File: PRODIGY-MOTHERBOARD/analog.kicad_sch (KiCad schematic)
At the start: 5 parts, among them U16 LM386

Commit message: CAN schematic done
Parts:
- renumbered R15 to R64, RV1 to RV3, U16 to U24
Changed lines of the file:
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@@
 		(dnp no)
 		(fields_autoplaced yes)
-		(property "Reference" "U16"
+		(property "Reference" "U24"
 			(at 72.39 140.0811 0)
 			(effects
@@
 			(project "PRODIGY-MOTHERBOARD"
 				(path "/f1c25860-8989-4190-bd24-2491d23ca7d9/a2bc12b1-b9d0-4419-aed0-74588fb36767"
-					(reference "U16")
+					(reference "U24")
 					(unit 1)
 				)
@@
 		(dnp no)
 		(fields_autoplaced yes)
-		(property "Reference" "RV1"
+		(property "Reference" "RV3"
 			(at 115.57 95.885 0)
 			(effects
@@
 			(project "PRODIGY-MOTHERBOARD"
 				(path "/f1c25860-8989-4190-bd24-2491d23ca7d9/a2bc12b1-b9d0-4419-aed0-74588fb36767"
-					(reference "RV1")
+					(reference "RV3")
 					(unit 1)
 				)
@@
 		(dnp no)
 		(fields_autoplaced yes)
-		(property "Reference" "R15"
+		(property "Reference" "R64"
 			(at 196.85 95.885 0)
 			(effects
@@
 			(project "PRODIGY-MOTHERBOARD"
 				(path "/f1c25860-8989-4190-bd24-2491d23ca7d9/a2bc12b1-b9d0-4419-aed0-74588fb36767"
-					(reference "R15")
-					(unit 1)
-				)
+					(reference "R64")
+					(unit 1)
+				)

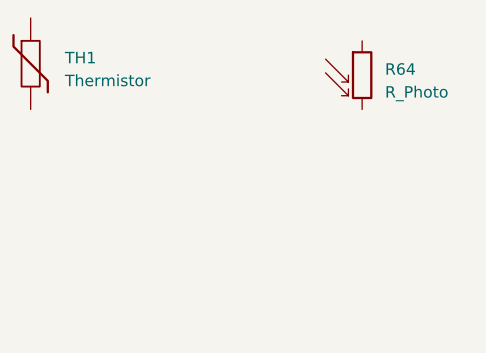
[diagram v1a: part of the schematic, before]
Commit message: SPI NFC schematic done.
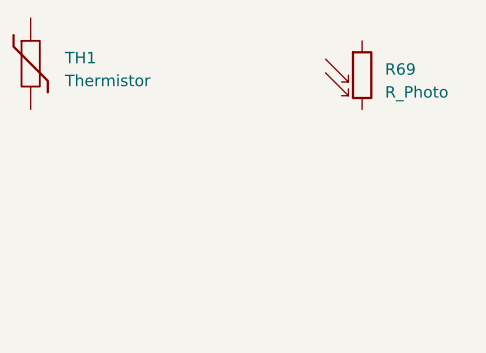
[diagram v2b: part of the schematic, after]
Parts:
- renumbered R64 to R69
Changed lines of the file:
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@@
 		(dnp no)
 		(fields_autoplaced yes)
-		(property "Reference" "R64"
+		(property "Reference" "R69"
 			(at 196.85 95.885 0)
 			(effects
@@
 			(project "PRODIGY-MOTHERBOARD"
 				(path "/f1c25860-8989-4190-bd24-2491d23ca7d9/a2bc12b1-b9d0-4419-aed0-74588fb36767"
-					(reference "R64")
+					(reference "R69")
 					(unit 1)
 				)

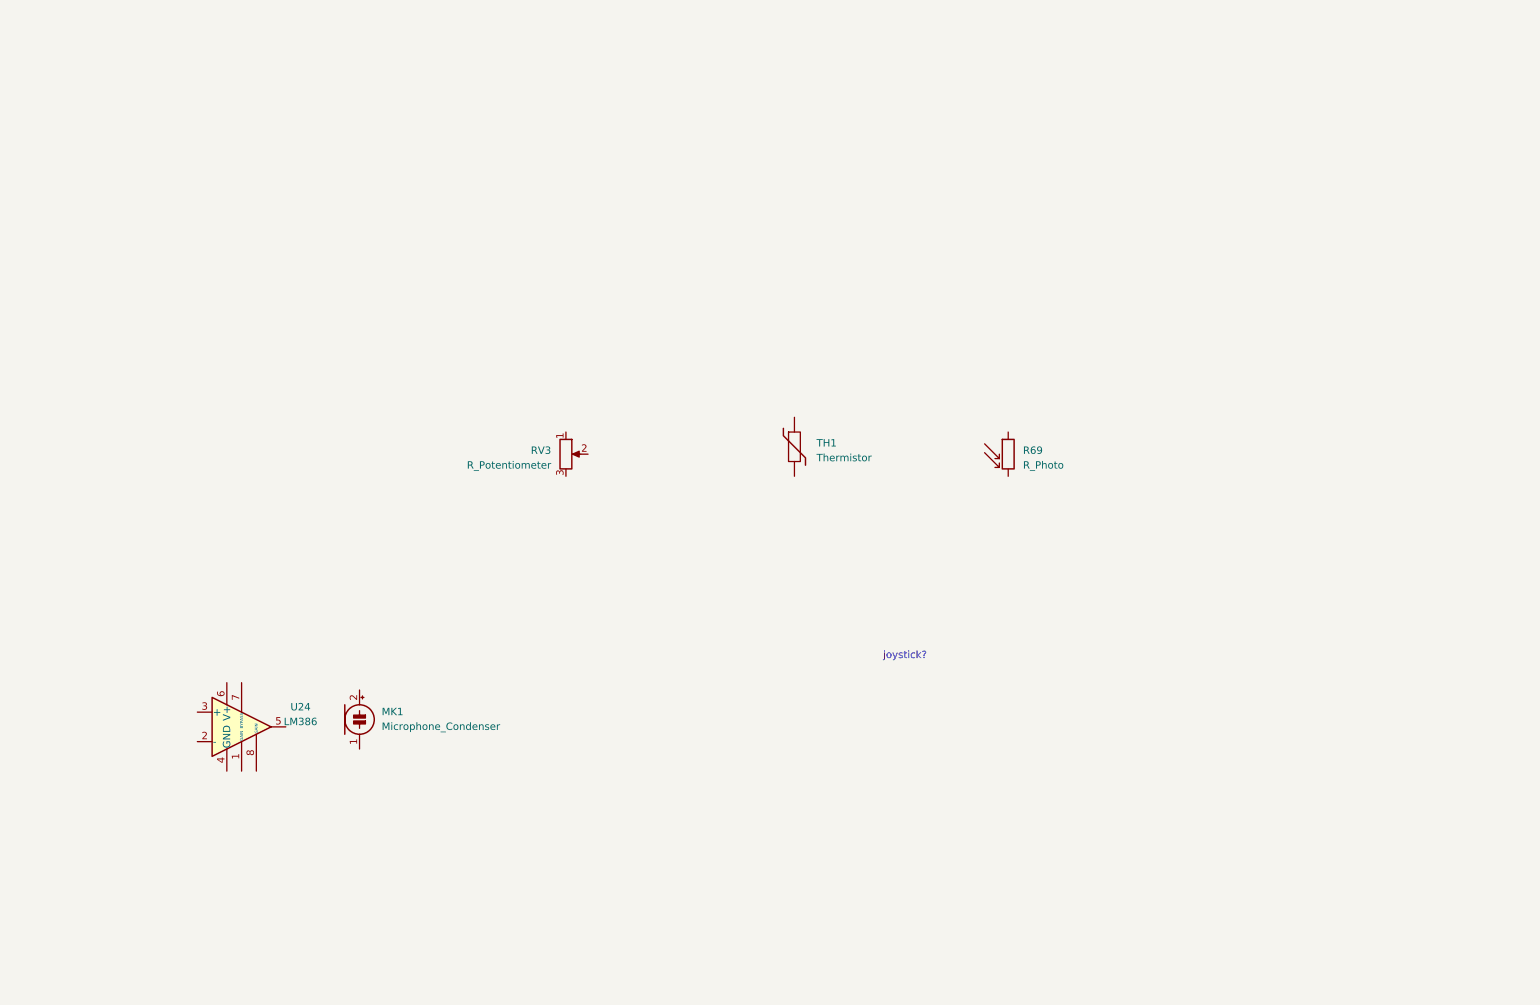
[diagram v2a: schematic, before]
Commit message: Analog schematic finished, except the joystick part.
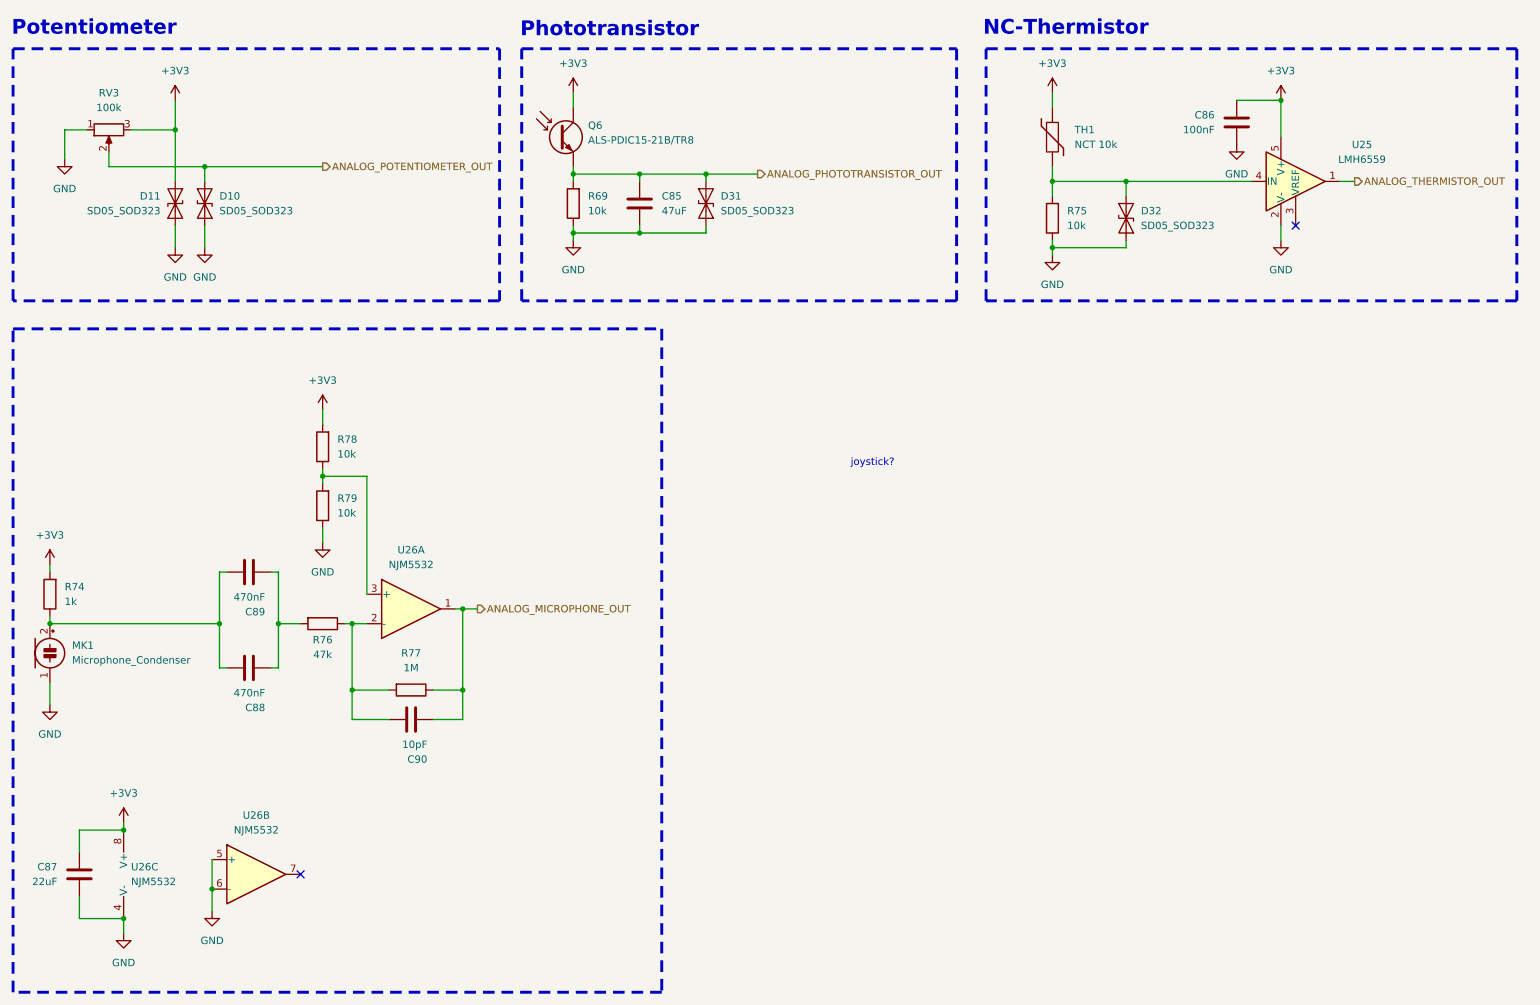
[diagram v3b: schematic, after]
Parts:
- removed R69: R_Photo, OptoDevice:R_LDR_5.1x4.3mm_P3.4mm_Vertical, symbol Device:R_Photo
- removed U24: LM386, Package_SO:SOP-8_3.9x4.9mm_P1.27mm, symbol Amplifier_Audio:LM386
- added C85: 47uF, symbol Device:C
- added C86: 100nF, symbol Device:C
- added C87: 22uF, symbol Device:C
- added C88, C89: 470nF, symbol Device:C
- added C90: 10pF, symbol Device:C
- added D10, D11, D31, D32: SD05_SOD323, Diode_SMD:D_SOD-323, symbol Diode:SD05_SOD323
- added Q6: ALS-PDIC15-21B/TR8, OptoDevice:Kingbright_KPS-3227, symbol Sensor_Optical:KPS-3227
- added R69, R75, R78, R79: 10k, symbol Device:R
- added R74: 1k, symbol Device:R
- added R76: 47k, symbol Device:R
- added R77: 1M, symbol Device:R
- added U25: LMH6559, Package_TO_SOT_SMD:SOT-23-5, symbol Amplifier_Buffer:BUF602xDBV
- added U26: NJM5532, symbol Amplifier_Operational:NJM5532
- RV3: value R_Potentiometer -> 100k; footprint Potentiometer_THT:Potentiometer_Piher_PT-15-V15_Vertical -> Potentiometer_THT:Potentiometer_Piher_PT-6-V_Vertical
- TH1: value Thermistor -> NCT 10k; footprint Package_TO_SOT_THT:TO-92_Inline_W4.0mm_Horizontal_FlatSideUp -> Resistor_SMD:R_0805_2012Metric
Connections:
- net +3V3: now reaches TH1.1
- net +3V3: now also RV3.3, C86.1, C87.1, D11.2 (A2), Q6.1, Q6.3, R74.2, R78.2, U25.5 (V+), U26.8 (V+)
- net at TH1.2: now also D32.2 (A2), R75.2, U25.4 (IN)
- net GND: now reaches RV3.1
- net GND: now also MK1.1 (-), C85.2, C86.2, C87.2, D10.1 (A1), D11.1 (A1), D31.1 (A1), D32.1 (A1), R69.1, R75.1, R79.1, U25.2 (V-), U26.4 (V-), U26.5 (+), U26.6 (-)
- net ANALOG_POTENTIOMETER_OUT: now reaches RV3.2
- net ANALOG_POTENTIOMETER_OUT: now also D10.2 (A2)
- net at MK1.2 (+): now also C88.1, C89.1, R74.1
- new net: C90.1, R76.1, R77.2, U26.2 (-)
- new net: C88.2, C89.2, R76.2
- new net: R78.1, R79.2, U26.3 (+)
- new net ANALOG_MICROPHONE_OUT: C90.2, R77.1, U26.1
- new net ANALOG_PHOTOTRANSISTOR_OUT: C85.1, D31.2 (A2), Q6.2, Q6.4, R69.2
- new net ANALOG_THERMISTOR_OUT: U25.1
- no-connect marks 0 -> 2
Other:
- note added: "NC-Thermistor"
- note added: "Phototransistor"
- note added: "Potentiometer"
- moved on the sheet: MK1, RV3, TH1

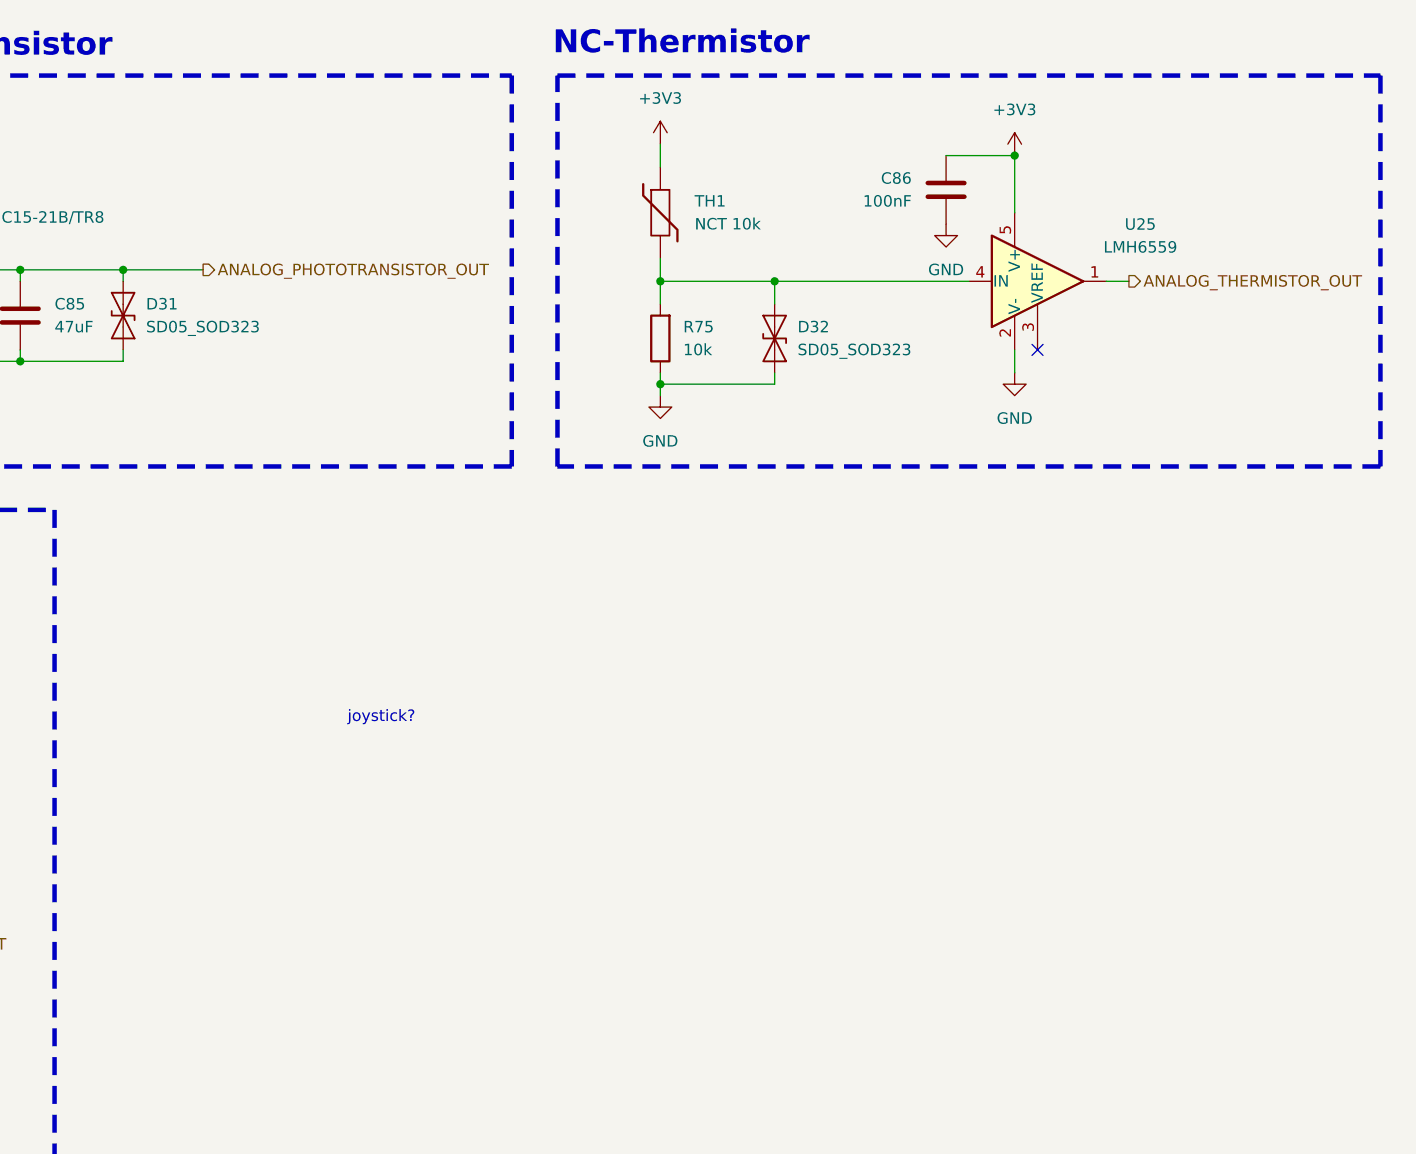
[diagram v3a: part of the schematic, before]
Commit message: 2-axis joystick footprint and sybmbol created. Analog-side done.
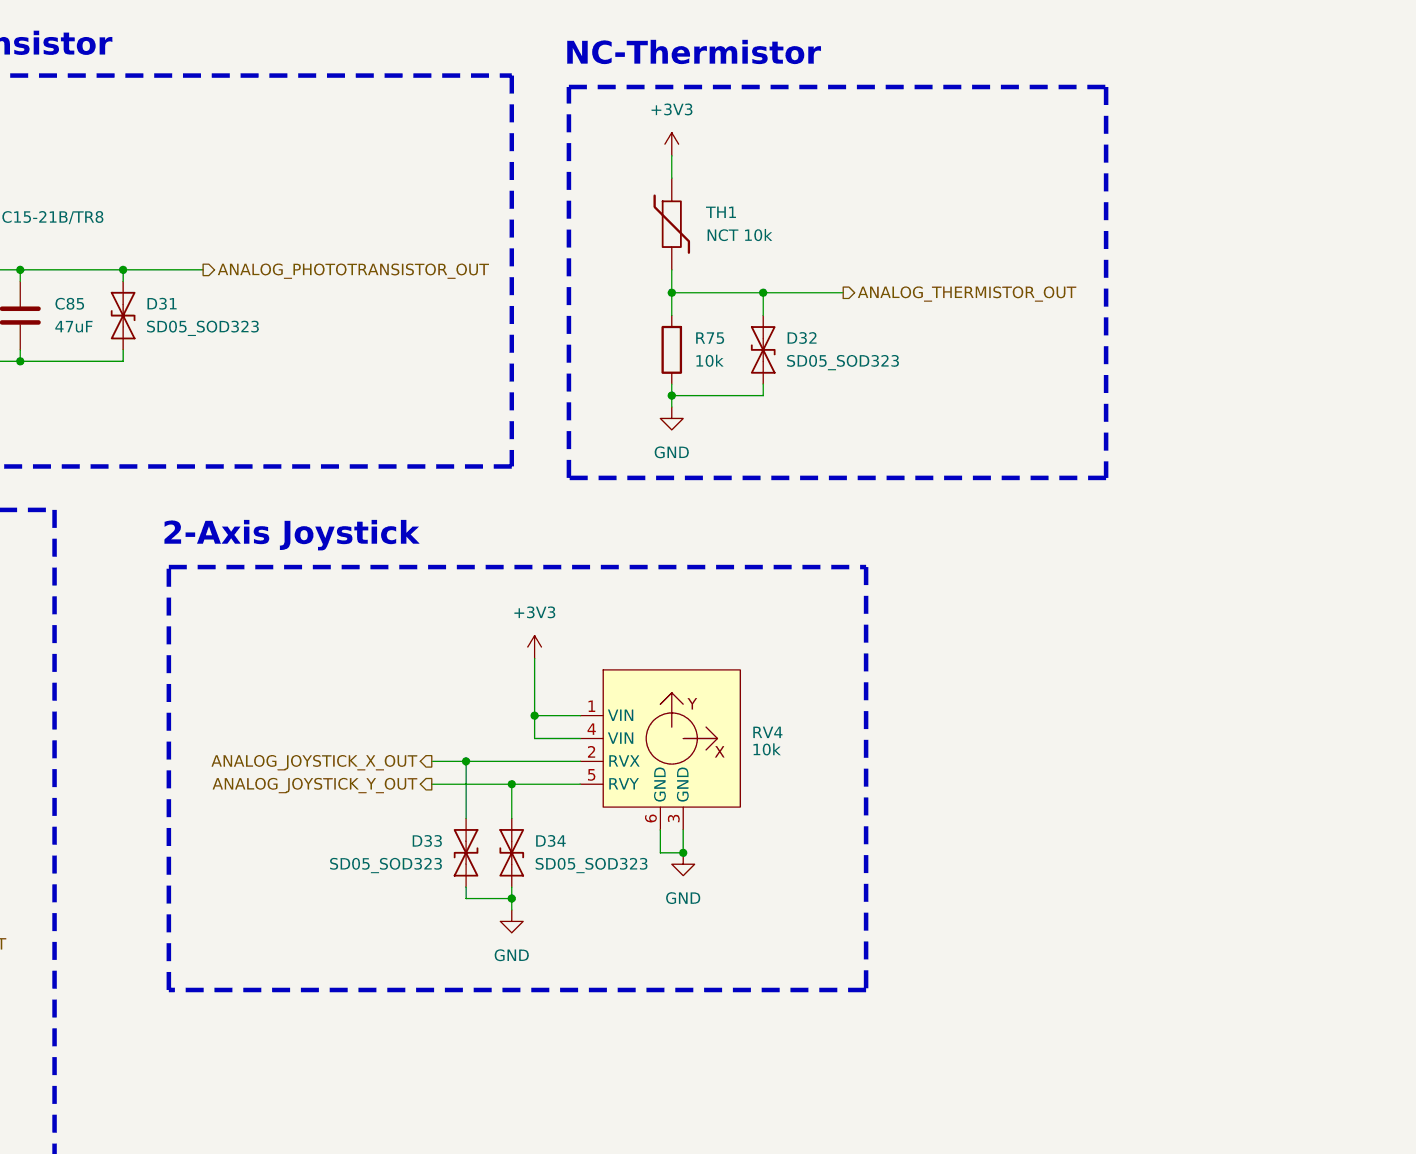
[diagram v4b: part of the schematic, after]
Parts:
- removed C86: 100nF, symbol Device:C
- removed U25: LMH6559, Package_TO_SOT_SMD:SOT-23-5, symbol Amplifier_Buffer:BUF602xDBV
- added D33, D34: SD05_SOD323, Diode_SMD:D_SOD-323, symbol Diode:SD05_SOD323
- added RV4: 10k, potentiometer_2_axis_joystick:2-Axis-Joystick, symbol potentiometer_2_axis_joystick:2-Axis-Joystick
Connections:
- net +3V3: now also RV4.1 (VIN), RV4.4 (VIN)
- net ANALOG_THERMISTOR_OUT: now also D32.2 (A2), R75.2, TH1.2
- net GND: now also D33.1 (A1), D34.1 (A1), RV4.3 (GND), RV4.6 (GND)
- new net ANALOG_JOYSTICK_X_OUT: D33.2 (A2), RV4.2 (RVX)
- new net ANALOG_JOYSTICK_Y_OUT: D34.2 (A2), RV4.5 (RVY)
- no-connect marks 2 -> 1
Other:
- note added: "2-Axis Joystick"
- note removed: "joystick?"
- moved on the sheet: D32, R75, TH1
